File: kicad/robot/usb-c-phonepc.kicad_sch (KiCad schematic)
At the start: 11 parts

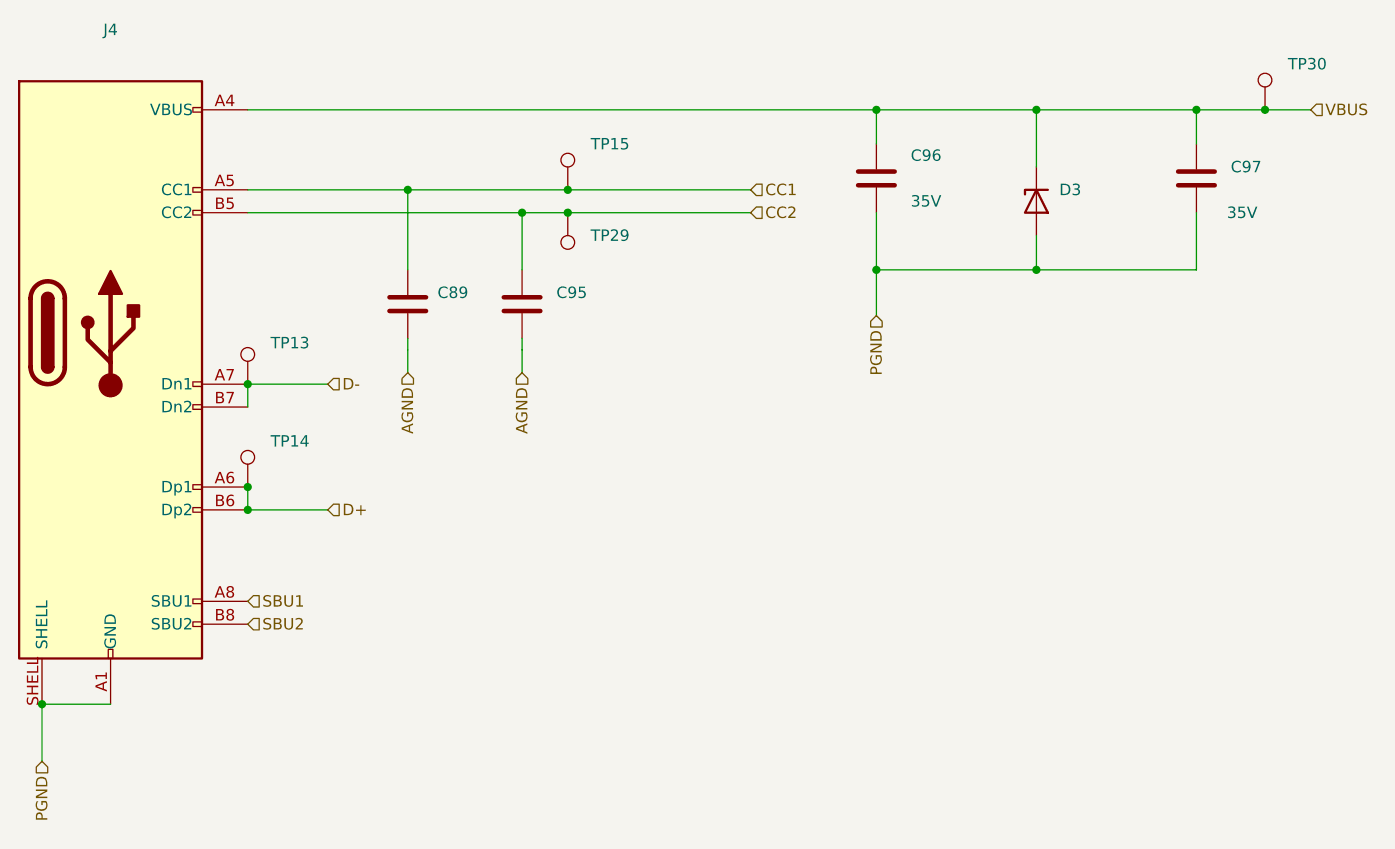
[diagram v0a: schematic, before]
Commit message: MAJOR REVISION. MAX77958 moved to new sheet and 2nd USB connector added
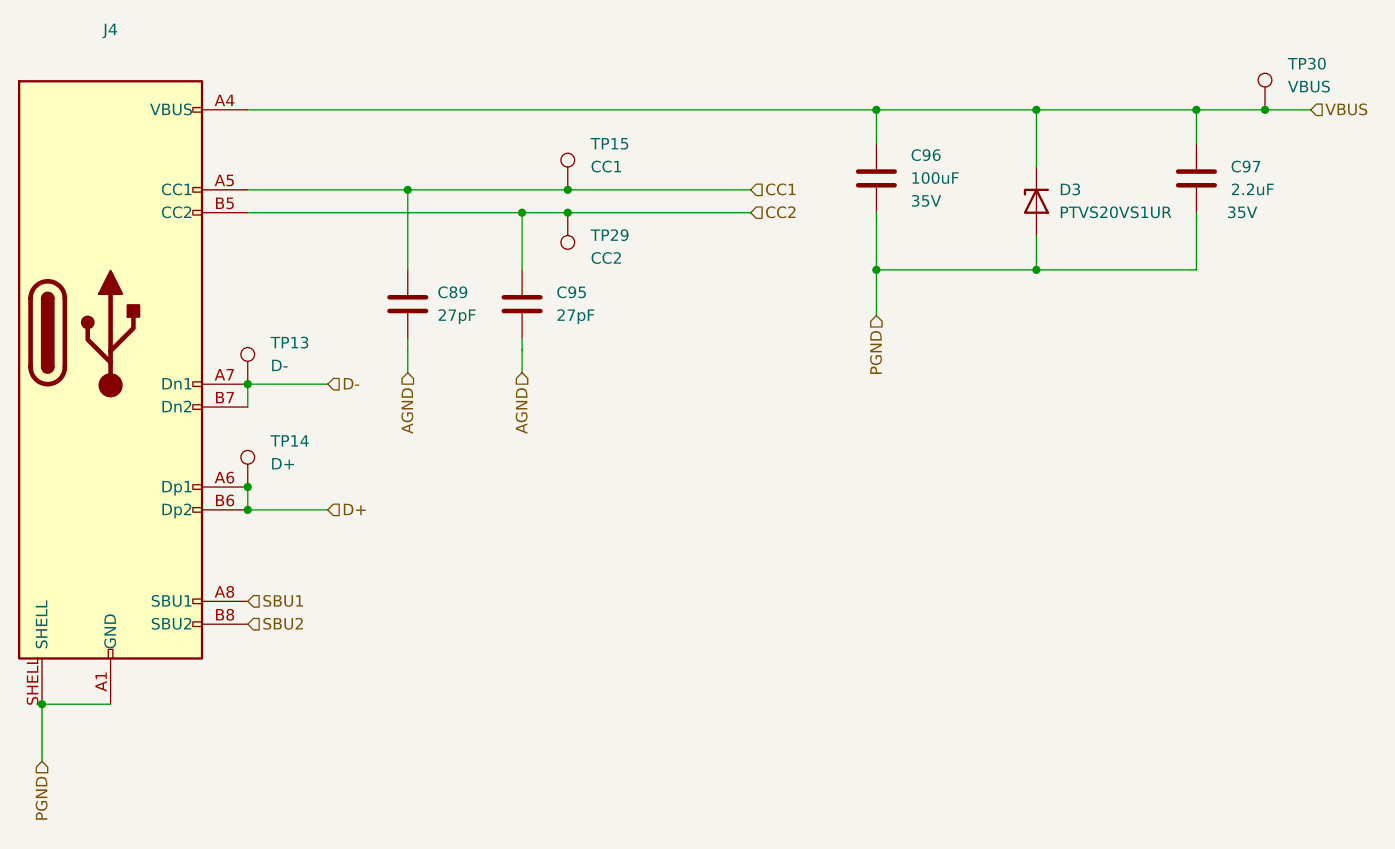
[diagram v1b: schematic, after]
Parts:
- C89, C95: value (none) -> 27pF; footprint (none) -> Capacitor_SMD:C_0402_1005Metric
- C96: value (none) -> 100uF; footprint (none) -> Capacitor_SMD:C_1210_3225Metric
- C97: value (none) -> 2.2uF; footprint (none) -> Capacitor_SMD:C_0805_2012Metric
- D3: value (none) -> PTVS20VS1UR; footprint (none) -> Diode_SMD:Nexperia_CFP3_SOD-123W
- J4: value (none) -> USB4120-03-C_REVA; footprint (none) -> Connector_USB:GCT_USB4120-03-C_REVA
- TP13: value (none) -> D-; footprint (none) -> TestPoint:KEYSTONE_5002
- TP14: value (none) -> D+; footprint (none) -> TestPoint:KEYSTONE_5002
- TP15: value (none) -> CC1; footprint (none) -> TestPoint:KEYSTONE_5002
- TP29: value (none) -> CC2; footprint (none) -> TestPoint:KEYSTONE_5002
- TP30: value (none) -> VBUS; footprint (none) -> TestPoint:KEYSTONE_5002
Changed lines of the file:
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@@
     (in_bom yes) (on_board yes) (fields_autoplaced)
     (property "Reference" "J4" (id 0) (at 91.44 62.23 0))
-    (property "Value" "" (id 1) (at 81.915 62.23 0)
-      (effects (font (size 1.27 1.27)) (justify left bottom) hide)
-    )
-    (property "Footprint" "" (id 2) (at 91.44 96.52 0)
+    (property "Value" "USB4120-03-C_REVA" (id 1) (at 81.915 62.23 0)
+      (effects (font (size 1.27 1.27)) (justify left bottom) hide)
+    )
+    (property "Footprint" "Connector_USB:GCT_USB4120-03-C_REVA" (id 2) (at 91.44 96.52 0)
       (effects (font (size 1.27 1.27)) (justify left bottom) hide)
     )
@@
       (effects (font (size 1.27 1.27)) (justify left))
     )
-    (property "Value" "" (id 1) (at 215.9 80.0099 0)
-      (effects (font (size 1.27 1.27)) (justify left))
-    )
-    (property "Footprint" "" (id 2) (at 213.0552 82.55 0)
+    (property "Value" "2.2uF" (id 1) (at 215.9 80.0099 0)
+      (effects (font (size 1.27 1.27)) (justify left))
+    )
+    (property "Footprint" "Capacitor_SMD:C_0805_2012Metric" (id 2) (at 213.0552 82.55 0)
       (effects (font (size 1.27 1.27)) hide)
     )
@@
       (effects (font (size 1.27 1.27)) (justify left))
     )
-    (property "Value" "" (id 1) (at 222.25 68.58 0)
-      (effects (font (size 1.27 1.27)) (justify left))
-    )
-    (property "Footprint" "" (id 2) (at 224.79 71.12 0)
+    (property "Value" "VBUS" (id 1) (at 222.25 68.58 0)
+      (effects (font (size 1.27 1.27)) (justify left))
+    )
+    (property "Footprint" "TestPoint:KEYSTONE_5002" (id 2) (at 224.79 71.12 0)
       (effects (font (size 1.27 1.27)) hide)
     )
@@
       (effects (font (size 1.27 1.27)) (justify left))
     )
-    (property "Value" "" (id 1) (at 180.34 78.7399 0)
-      (effects (font (size 1.27 1.27)) (justify left))
-    )
-    (property "Footprint" "" (id 2) (at 177.4952 82.55 0)
+    (property "Value" "100uF" (id 1) (at 180.34 78.7399 0)
+      (effects (font (size 1.27 1.27)) (justify left))
+    )
+    (property "Footprint" "Capacitor_SMD:C_1210_3225Metric" (id 2) (at 177.4952 82.55 0)
       (effects (font (size 1.27 1.27)) hide)
     )
@@
       (effects (font (size 1.27 1.27)) (justify left))
     )
-    (property "Value" "" (id 1) (at 144.78 77.47 0)
-      (effects (font (size 1.27 1.27)) (justify left))
-    )
-    (property "Footprint" "" (id 2) (at 147.32 80.01 0)
+    (property "Value" "CC1" (id 1) (at 144.78 77.47 0)
+      (effects (font (size 1.27 1.27)) (justify left))
+    )
+    (property "Footprint" "TestPoint:KEYSTONE_5002" (id 2) (at 147.32 80.01 0)
       (effects (font (size 1.27 1.27)) hide)
     )
@@
       (effects (font (size 1.27 1.27)) (justify right))
     )
-    (property "Value" "" (id 1) (at 196.85 82.5499 90)
-      (effects (font (size 1.27 1.27)) (justify right))
-    )
-    (property "Footprint" "" (id 2) (at 194.31 81.28 0)
+    (property "Value" "PTVS20VS1UR" (id 1) (at 196.85 82.5499 90)
+      (effects (font (size 1.27 1.27)) (justify right))
+    )
+    (property "Footprint" "Diode_SMD:Nexperia_CFP3_SOD-123W" (id 2) (at 194.31 81.28 0)
       (effects (font (size 1.27 1.27)) hide)
     )
@@
       (effects (font (size 1.27 1.27)) (justify left))
     )
-    (property "Value" "" (id 1) (at 109.22 110.49 0)
-      (effects (font (size 1.27 1.27)) (justify left))
-    )
-    (property "Footprint" "" (id 2) (at 111.76 113.03 0)
+    (property "Value" "D+" (id 1) (at 109.22 110.49 0)
+      (effects (font (size 1.27 1.27)) (justify left))
+    )
+    (property "Footprint" "TestPoint:KEYSTONE_5002" (id 2) (at 111.76 113.03 0)
       (effects (font (size 1.27 1.27)) hide)
     )
@@
       (effects (font (size 1.27 1.27)) (justify left))
     )
-    (property "Value" "" (id 1) (at 140.97 93.9799 0)
-      (effects (font (size 1.27 1.27)) (justify left))
-    )
-    (property "Footprint" "" (id 2) (at 138.1252 96.52 0)
+    (property "Value" "27pF" (id 1) (at 140.97 93.9799 0)
+      (effects (font (size 1.27 1.27)) (justify left))
+    )
+    (property "Footprint" "Capacitor_SMD:C_0402_1005Metric" (id 2) (at 138.1252 96.52 0)
       (effects (font (size 1.27 1.27)) hide)
     )
@@
       (effects (font (size 1.27 1.27)) (justify left))
     )
-    (property "Value" "" (id 1) (at 109.22 99.5679 0)
-      (effects (font (size 1.27 1.27)) (justify left))
-    )
-    (property "Footprint" "" (id 2) (at 111.76 101.6 0)
+    (property "Value" "D-" (id 1) (at 109.22 99.5679 0)
+      (effects (font (size 1.27 1.27)) (justify left))
+    )
+    (property "Footprint" "TestPoint:KEYSTONE_5002" (id 2) (at 111.76 101.6 0)
       (effects (font (size 1.27 1.27)) hide)
     )
@@
       (effects (font (size 1.27 1.27)) (justify left))
     )
-    (property "Value" "" (id 1) (at 127.762 93.98 0)
-      (effects (font (size 1.27 1.27)) (justify left))
-    )
-    (property "Footprint" "" (id 2) (at 125.4252 96.52 0)
+    (property "Value" "27pF" (id 1) (at 127.762 93.98 0)
+      (effects (font (size 1.27 1.27)) (justify left))
+    )
+    (property "Footprint" "Capacitor_SMD:C_0402_1005Metric" (id 2) (at 125.4252 96.52 0)
       (effects (font (size 1.27 1.27)) hide)
     )
@@
       (effects (font (size 1.27 1.27)) (justify right))
     )
-    (property "Value" "" (id 1) (at 144.78 87.63 0)
-      (effects (font (size 1.27 1.27)) (justify right))
-    )
-    (property "Footprint" "" (id 2) (at 137.16 82.55 0)
-      (effects (font (size 1.27 1.27)) hide)
-    )
+    (property "Value" "CC2" (id 1) (at 144.78 87.63 0)
+      (effects (font (size 1.27 1.27)) (justify right))
+    )
+    (property "Footprint" "TestPoint:KEYSTONE_5002" (id 2) (at 137.16 82.55 0)
+      (effects (font (size 1.27 1.27)) hide)
+    )

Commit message: Renamed USB sheets
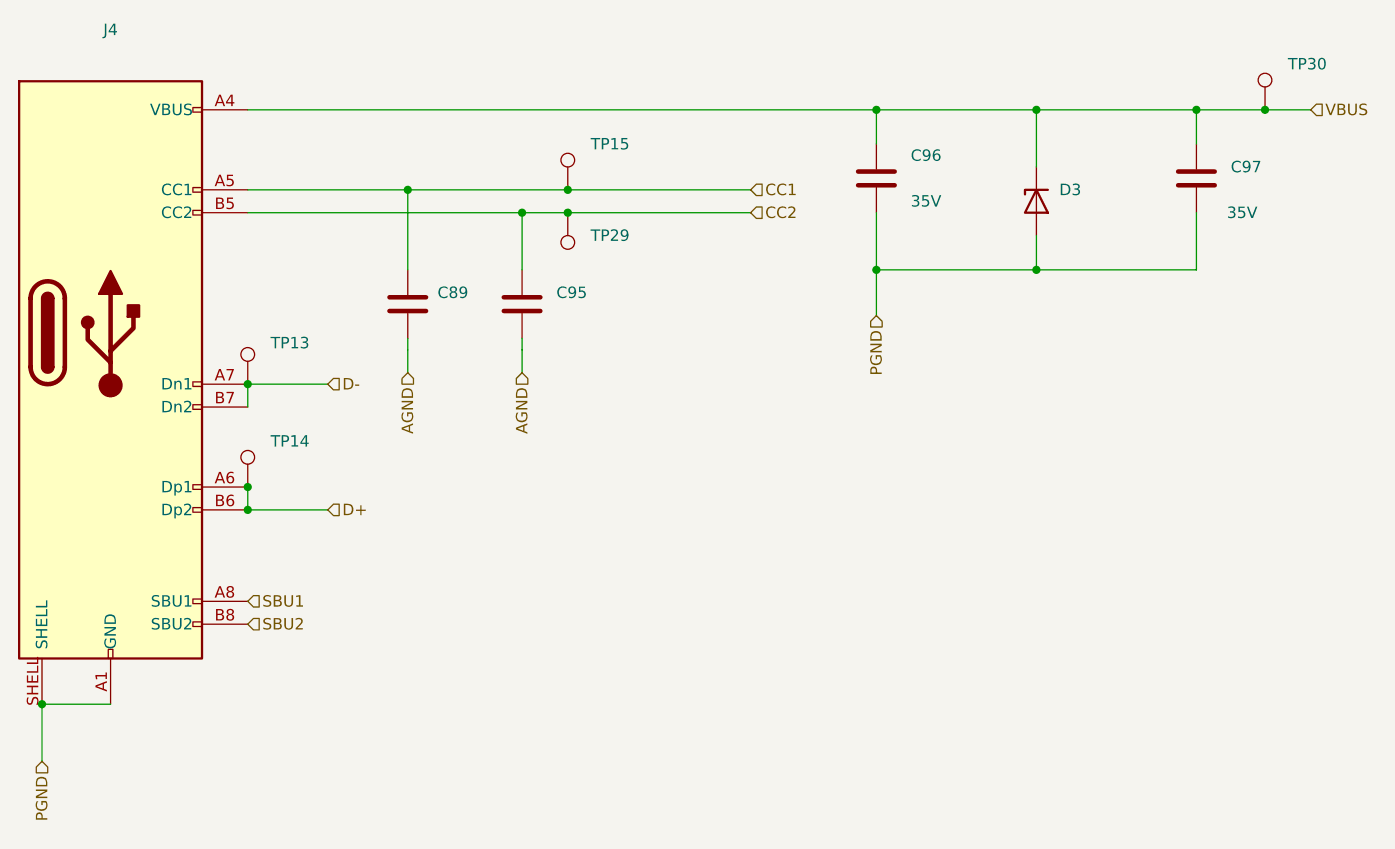
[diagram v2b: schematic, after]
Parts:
- C89, C95: value 27pF -> (none); footprint Capacitor_SMD:C_0402_1005Metric -> (none)
- C96: value 100uF -> (none); footprint Capacitor_SMD:C_1210_3225Metric -> (none)
- C97: value 2.2uF -> (none); footprint Capacitor_SMD:C_0805_2012Metric -> (none)
- D3: value PTVS20VS1UR -> (none); footprint Diode_SMD:Nexperia_CFP3_SOD-123W -> (none)
- J4: value USB4120-03-C_REVA -> (none); footprint Connector_USB:GCT_USB4120-03-C_REVA -> (none)
- TP13: value D- -> (none); footprint TestPoint:KEYSTONE_5002 -> (none)
- TP14: value D+ -> (none); footprint TestPoint:KEYSTONE_5002 -> (none)
- TP15: value CC1 -> (none); footprint TestPoint:KEYSTONE_5002 -> (none)
- TP29: value CC2 -> (none); footprint TestPoint:KEYSTONE_5002 -> (none)
- TP30: value VBUS -> (none); footprint TestPoint:KEYSTONE_5002 -> (none)
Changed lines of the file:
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@@
     (in_bom yes) (on_board yes) (fields_autoplaced)
     (property "Reference" "J4" (id 0) (at 91.44 62.23 0))
-    (property "Value" "USB4120-03-C_REVA" (id 1) (at 81.915 62.23 0)
-      (effects (font (size 1.27 1.27)) (justify left bottom) hide)
-    )
-    (property "Footprint" "Connector_USB:GCT_USB4120-03-C_REVA" (id 2) (at 91.44 96.52 0)
+    (property "Value" "" (id 1) (at 81.915 62.23 0)
+      (effects (font (size 1.27 1.27)) (justify left bottom) hide)
+    )
+    (property "Footprint" "" (id 2) (at 91.44 96.52 0)
       (effects (font (size 1.27 1.27)) (justify left bottom) hide)
     )
@@
       (effects (font (size 1.27 1.27)) (justify left))
     )
-    (property "Value" "2.2uF" (id 1) (at 215.9 80.0099 0)
-      (effects (font (size 1.27 1.27)) (justify left))
-    )
-    (property "Footprint" "Capacitor_SMD:C_0805_2012Metric" (id 2) (at 213.0552 82.55 0)
+    (property "Value" "" (id 1) (at 215.9 80.0099 0)
+      (effects (font (size 1.27 1.27)) (justify left))
+    )
+    (property "Footprint" "" (id 2) (at 213.0552 82.55 0)
       (effects (font (size 1.27 1.27)) hide)
     )
@@
       (effects (font (size 1.27 1.27)) (justify left))
     )
-    (property "Value" "VBUS" (id 1) (at 222.25 68.58 0)
-      (effects (font (size 1.27 1.27)) (justify left))
-    )
-    (property "Footprint" "TestPoint:KEYSTONE_5002" (id 2) (at 224.79 71.12 0)
+    (property "Value" "" (id 1) (at 222.25 68.58 0)
+      (effects (font (size 1.27 1.27)) (justify left))
+    )
+    (property "Footprint" "" (id 2) (at 224.79 71.12 0)
       (effects (font (size 1.27 1.27)) hide)
     )
@@
       (effects (font (size 1.27 1.27)) (justify left))
     )
-    (property "Value" "100uF" (id 1) (at 180.34 78.7399 0)
-      (effects (font (size 1.27 1.27)) (justify left))
-    )
-    (property "Footprint" "Capacitor_SMD:C_1210_3225Metric" (id 2) (at 177.4952 82.55 0)
+    (property "Value" "" (id 1) (at 180.34 78.7399 0)
+      (effects (font (size 1.27 1.27)) (justify left))
+    )
+    (property "Footprint" "" (id 2) (at 177.4952 82.55 0)
       (effects (font (size 1.27 1.27)) hide)
     )
@@
       (effects (font (size 1.27 1.27)) (justify left))
     )
-    (property "Value" "CC1" (id 1) (at 144.78 77.47 0)
-      (effects (font (size 1.27 1.27)) (justify left))
-    )
-    (property "Footprint" "TestPoint:KEYSTONE_5002" (id 2) (at 147.32 80.01 0)
+    (property "Value" "" (id 1) (at 144.78 77.47 0)
+      (effects (font (size 1.27 1.27)) (justify left))
+    )
+    (property "Footprint" "" (id 2) (at 147.32 80.01 0)
       (effects (font (size 1.27 1.27)) hide)
     )
@@
       (effects (font (size 1.27 1.27)) (justify right))
     )
-    (property "Value" "PTVS20VS1UR" (id 1) (at 196.85 82.5499 90)
-      (effects (font (size 1.27 1.27)) (justify right))
-    )
-    (property "Footprint" "Diode_SMD:Nexperia_CFP3_SOD-123W" (id 2) (at 194.31 81.28 0)
+    (property "Value" "" (id 1) (at 196.85 82.5499 90)
+      (effects (font (size 1.27 1.27)) (justify right))
+    )
+    (property "Footprint" "" (id 2) (at 194.31 81.28 0)
       (effects (font (size 1.27 1.27)) hide)
     )
@@
       (effects (font (size 1.27 1.27)) (justify left))
     )
-    (property "Value" "D+" (id 1) (at 109.22 110.49 0)
-      (effects (font (size 1.27 1.27)) (justify left))
-    )
-    (property "Footprint" "TestPoint:KEYSTONE_5002" (id 2) (at 111.76 113.03 0)
+    (property "Value" "" (id 1) (at 109.22 110.49 0)
+      (effects (font (size 1.27 1.27)) (justify left))
+    )
+    (property "Footprint" "" (id 2) (at 111.76 113.03 0)
       (effects (font (size 1.27 1.27)) hide)
     )
@@
       (effects (font (size 1.27 1.27)) (justify left))
     )
-    (property "Value" "27pF" (id 1) (at 140.97 93.9799 0)
-      (effects (font (size 1.27 1.27)) (justify left))
-    )
-    (property "Footprint" "Capacitor_SMD:C_0402_1005Metric" (id 2) (at 138.1252 96.52 0)
+    (property "Value" "" (id 1) (at 140.97 93.9799 0)
+      (effects (font (size 1.27 1.27)) (justify left))
+    )
+    (property "Footprint" "" (id 2) (at 138.1252 96.52 0)
       (effects (font (size 1.27 1.27)) hide)
     )
@@
       (effects (font (size 1.27 1.27)) (justify left))
     )
-    (property "Value" "D-" (id 1) (at 109.22 99.5679 0)
-      (effects (font (size 1.27 1.27)) (justify left))
-    )
-    (property "Footprint" "TestPoint:KEYSTONE_5002" (id 2) (at 111.76 101.6 0)
+    (property "Value" "" (id 1) (at 109.22 99.5679 0)
+      (effects (font (size 1.27 1.27)) (justify left))
+    )
+    (property "Footprint" "" (id 2) (at 111.76 101.6 0)
       (effects (font (size 1.27 1.27)) hide)
     )
@@
       (effects (font (size 1.27 1.27)) (justify left))
     )
-    (property "Value" "27pF" (id 1) (at 127.762 93.98 0)
-      (effects (font (size 1.27 1.27)) (justify left))
-    )
-    (property "Footprint" "Capacitor_SMD:C_0402_1005Metric" (id 2) (at 125.4252 96.52 0)
+    (property "Value" "" (id 1) (at 127.762 93.98 0)
+      (effects (font (size 1.27 1.27)) (justify left))
+    )
+    (property "Footprint" "" (id 2) (at 125.4252 96.52 0)
       (effects (font (size 1.27 1.27)) hide)
     )
@@
       (effects (font (size 1.27 1.27)) (justify right))
     )
-    (property "Value" "CC2" (id 1) (at 144.78 87.63 0)
-      (effects (font (size 1.27 1.27)) (justify right))
-    )
-    (property "Footprint" "TestPoint:KEYSTONE_5002" (id 2) (at 137.16 82.55 0)
-      (effects (font (size 1.27 1.27)) hide)
-    )
+    (property "Value" "" (id 1) (at 144.78 87.63 0)
+      (effects (font (size 1.27 1.27)) (justify right))
+    )
+    (property "Footprint" "" (id 2) (at 137.16 82.55 0)
+      (effects (font (size 1.27 1.27)) hide)
+    )
